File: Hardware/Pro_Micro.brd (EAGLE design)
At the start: 17.8 x 33 mm, 33 parts, among them U2 MIC5219, U3 ATMEGA32U4, Y1 16MHz

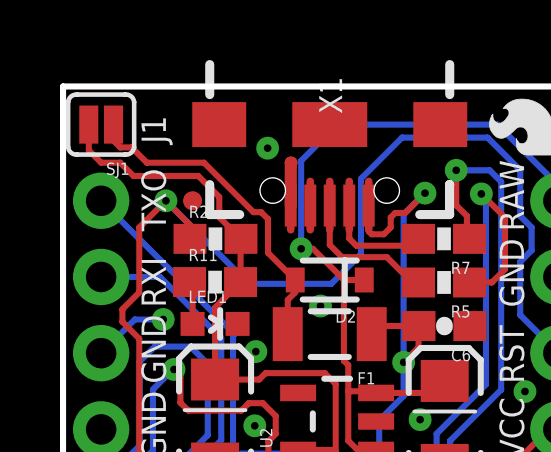
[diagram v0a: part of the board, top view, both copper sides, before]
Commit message: Changed jumper package to normally open
Open Jumper = 3.3V logic

also added gitignore
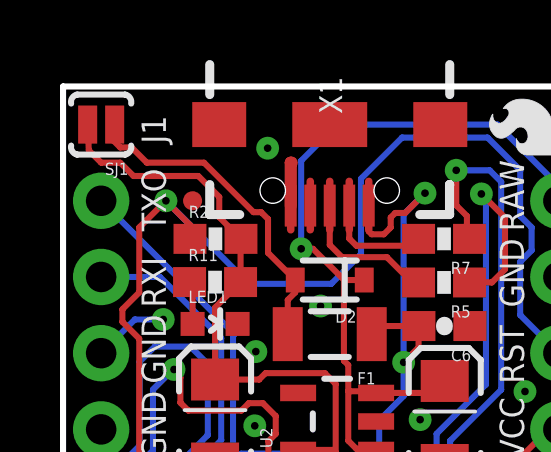
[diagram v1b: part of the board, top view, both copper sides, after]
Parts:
- SJ1: device SparkFun:SJ_2S -> SparkFun:SJ_2S-NO

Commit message: repositioned fiducials and one via
It used to be under the crystal.
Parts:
- moved JP2 13.1 mm to (17.0, 32.3)
- moved JP1 5.66 mm to (6.86, 6.10)
